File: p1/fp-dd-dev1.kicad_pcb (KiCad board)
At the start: 2 copper layers, 50.5 x 128.5 mm, 20 parts

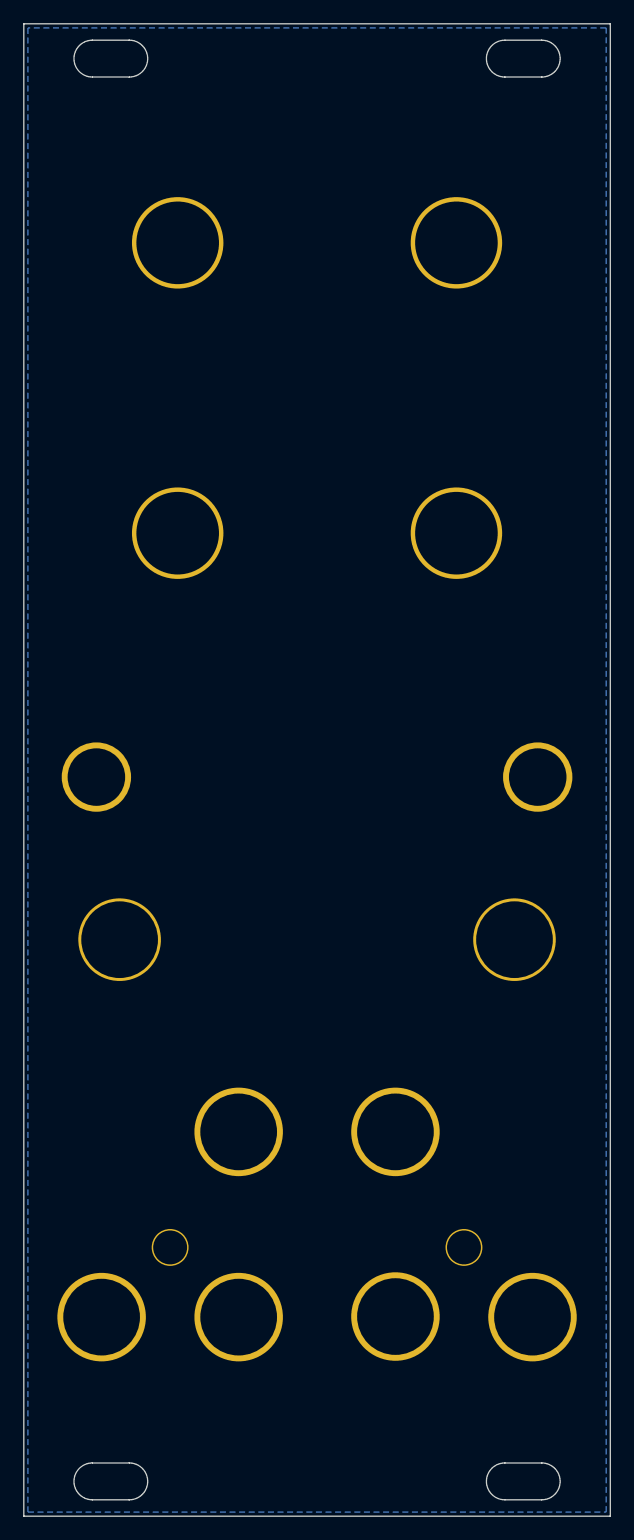
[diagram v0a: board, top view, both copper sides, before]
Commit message: plotted fp gerbers
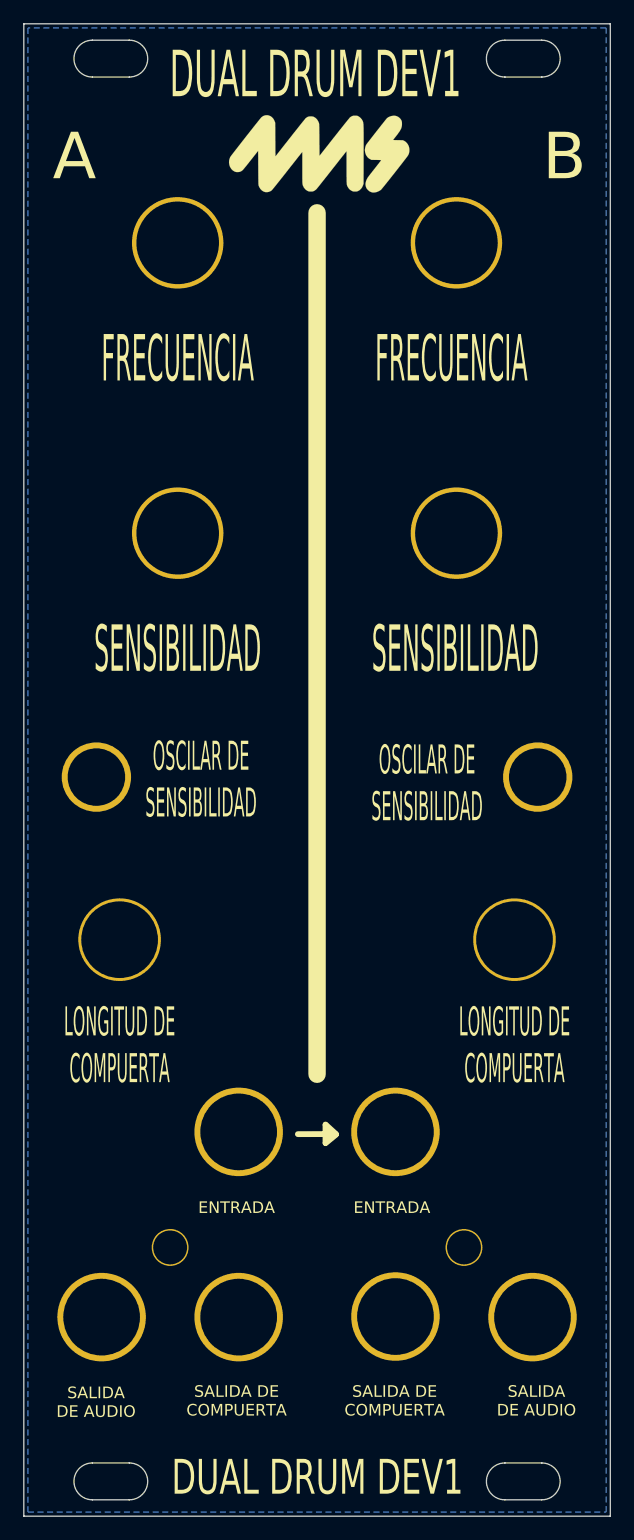
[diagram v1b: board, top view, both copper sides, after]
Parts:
- added G***: LOGO, 4ms_Symbol:4msLogo_15.5x6.6mm, F.Cu at (24.2, -107.7)
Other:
- board text added: "A"
- board text added: "B"
- board text added: "DUAL DRUM DEV1"
- board text added: "ENTRADA"
- board text added: "FRECUENCIA"
- board text added: "LONGITUD DE COMPUERTA"
- board text added: "OSCILAR DE SENSIBILIDAD"
- board text added: "SALIDA DE AUDIO"
- board text added: "SALIDA DE COMPUERTA"
- board text added: "SENSIBILIDAD"
